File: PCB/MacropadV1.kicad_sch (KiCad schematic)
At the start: 17 parts, among them J1 Conn_01x04, SW1 SW_Push, SW10 RotaryEncoder_Switch, SW2 SW_Push, SW3 SW_Push, SW4 SW_Push, SW5 SW_Push, SW6 SW_Push, U1 MOUDLE-SEEEDUINO-XIAO

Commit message: just making sure i didnt forget anything
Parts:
- D1, D2, D3, D4, D5, D6: value D -> 1N4148; footprint Crystal:Crystal_SMD_G8-2Pin_3.2x1.5mm -> Diode_SMD:D_SOD-123
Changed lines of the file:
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@@
 			)
 		)
-		(property "Value" "D"
+		(property "Value" "1N4148"
 			(at 158.75 64.7699 90)
 			(show_name no)
@@
 			)
 		)
-		(property "Footprint" "Crystal:Crystal_SMD_G8-2Pin_3.2x1.5mm"
+		(property "Footprint" "Diode_SMD:D_SOD-123"
 			(at 156.21 63.5 0)
 			(hide yes)
@@
 			)
 		)
-		(property "Value" "D"
+		(property "Value" "1N4148"
 			(at 186.69 64.7699 90)
 			(show_name no)
@@
 			)
 		)
-		(property "Footprint" "Crystal:Crystal_SMD_G8-2Pin_3.2x1.5mm"
+		(property "Footprint" "Diode_SMD:D_SOD-123"
 			(at 184.15 63.5 0)
 			(hide yes)
@@
 			)
 		)
-		(property "Value" "D"
+		(property "Value" "1N4148"
 			(at 158.75 91.4399 90)
 			(show_name no)
@@
 			)
 		)
-		(property "Footprint" "Crystal:Crystal_SMD_G8-2Pin_3.2x1.5mm"
+		(property "Footprint" "Diode_SMD:D_SOD-123"
 			(at 156.21 90.17 0)
 			(hide yes)
@@
 			)
 		)
-		(property "Value" "D"
+		(property "Value" "1N4148"
 			(at 186.69 91.4399 90)
 			(show_name no)
@@
 			)
 		)
-		(property "Footprint" "Crystal:Crystal_SMD_G8-2Pin_3.2x1.5mm"
+		(property "Footprint" "Diode_SMD:D_SOD-123"
 			(at 184.15 90.17 0)
 			(hide yes)
@@
 			)
 		)
-		(property "Value" "D"
+		(property "Value" "1N4148"
 			(at 158.75 78.7399 90)
 			(show_name no)
@@
 			)
 		)
-		(property "Footprint" "Crystal:Crystal_SMD_G8-2Pin_3.2x1.5mm"
+		(property "Footprint" "Diode_SMD:D_SOD-123"
 			(at 156.21 77.47 0)
 			(hide yes)
@@
 			)
 		)
-		(property "Value" "D"
+		(property "Value" "1N4148"
 			(at 186.69 78.7399 90)
 			(show_name no)
@@
 			)
 		)
-		(property "Footprint" "Crystal:Crystal_SMD_G8-2Pin_3.2x1.5mm"
+		(property "Footprint" "Diode_SMD:D_SOD-123"
 			(at 184.15 77.47 0)
 			(hide yes)

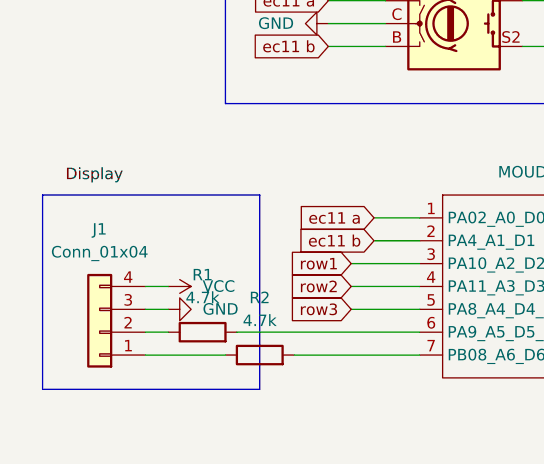
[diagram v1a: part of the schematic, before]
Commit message: fixed schematic display error
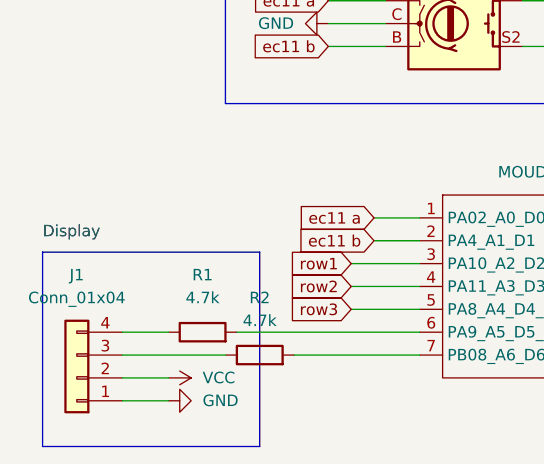
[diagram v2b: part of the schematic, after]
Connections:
- net GND: now also J1.1 (Pin_1); no longer J1.3 (Pin_3)
- net VCC: now also J1.2 (Pin_2); no longer J1.4 (Pin_4)
- net at R2.1: now also J1.3 (Pin_3); no longer J1.1 (Pin_1)
- net at R1.1: now also J1.4 (Pin_4); no longer J1.2 (Pin_2)
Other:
- moved on the sheet: J1
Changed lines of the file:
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@@
 	)
 	(rectangle
-		(start 33.02 77.47)
-		(end 57.15 99.06)
+		(start 33.02 83.82)
+		(end 57.15 105.41)
 		(stroke
 			(width 0)
@@
 	(wire
 		(pts
-			(xy 44.45 92.71) (xy 46.99 92.71)
-		)
-		(stroke
-			(width 0)
-			(type default)
-		)
-	)
-	(wire
-		(pts
 			(xy 67.31 90.17) (xy 74.93 90.17)
 		)
@@
 	(wire
 		(pts
-			(xy 44.45 95.25) (xy 53.34 95.25)
+			(xy 41.91 92.71) (xy 46.99 92.71)
 		)
 		(stroke
@@
 	(wire
 		(pts
-			(xy 44.45 90.17) (xy 46.99 90.17)
+			(xy 41.91 95.25) (xy 53.34 95.25)
 		)
 		(stroke
@@
 	(wire
 		(pts
+			(xy 41.91 97.79) (xy 46.99 97.79)
+		)
+		(stroke
+			(width 0)
+			(type default)
+		)
+	)
+	(wire
+		(pts
 			(xy 115.57 85.09) (xy 118.11 85.09)
 		)
@@
 	(wire
 		(pts
-			(xy 44.45 87.63) (xy 46.99 87.63)
-		)
-		(stroke
-			(width 0)
-			(type default)
-		)
-	)
-	(wire
-		(pts
 			(xy 184.15 86.36) (xy 187.96 86.36)
 		)
@@
 		(pts
 			(xy 184.15 59.69) (xy 187.96 59.69)
+		)
+		(stroke
+			(width 0)
+			(type default)
+		)
+	)
+	(wire
+		(pts
+			(xy 41.91 100.33) (xy 46.99 100.33)
 		)
 		(stroke
@@
 	)
 	(label "Display"
-		(at 35.56 76.2 0)
+		(at 33.02 82.55 0)
 		(effects
 			(font
@@
 	(symbol
 		(lib_id "Connector_Generic:Conn_01x04")
-		(at 39.37 92.71 180)
+		(at 36.83 97.79 180)
 		(unit 1)
 		(body_style 1)
@@
 		(fields_autoplaced yes)
 		(property "Reference" "J1"
-			(at 39.37 81.28 0)
+			(at 36.83 86.36 0)
 			(show_name no)
 			(do_not_autoplace no)
@@
 		)
 		(property "Value" "Conn_01x04"
-			(at 39.37 83.82 0)
+			(at 36.83 88.9 0)
 			(show_name no)
 			(do_not_autoplace no)
@@
 		)
 		(property "Footprint" "KicadMods:SSD1306-0.91-OLED-4pin-128x32"
-			(at 39.37 92.71 0)
+			(at 36.83 97.79 0)
 			(hide yes)
 			(show_name no)
@@
 		)
 		(property "Datasheet" ""
-			(at 39.37 92.71 0)
+			(at 36.83 97.79 0)
 			(hide yes)
 			(show_name no)
@@
 		)
 		(property "Description" "Generic connector, single row, 01x04, script generated (kicad-library-utils/schlib/autogen/connector/)"
-			(at 39.37 92.71 0)
+			(at 36.83 97.79 0)
 			(hide yes)
 			(show_name no)
@@
 	(symbol
 		(lib_id "power:VCC")
-		(at 46.99 87.63 270)
+		(at 46.99 97.79 270)
 		(unit 1)
 		(body_style 1)
@@
 		(fields_autoplaced yes)
 		(property "Reference" "#PWR03"
-			(at 43.18 87.63 0)
+			(at 43.18 97.79 0)
 			(hide yes)
 			(show_name no)
@@
 		)
 		(property "Value" "VCC"
-			(at 50.8 87.6299 90)
+			(at 50.8 97.7899 90)
 			(show_name no)
 			(do_not_autoplace no)
@@
 		)
 		(property "Footprint" ""
-			(at 46.99 87.63 0)
+			(at 46.99 97.79 0)
 			(hide yes)
 			(show_name no)
@@
 		)
 		(property "Datasheet" ""
-			(at 46.99 87.63 0)
+			(at 46.99 97.79 0)
 			(hide yes)
 			(show_name no)
@@
 		)
 		(property "Description" "Power symbol creates a global label with name \"VCC\""
-			(at 46.99 87.63 0)
+			(at 46.99 97.79 0)
 			(hide yes)
 			(show_name no)
@@
 	(symbol
 		(lib_id "power:GND")
-		(at 46.99 90.17 90)
+		(at 46.99 100.33 90)
 		(unit 1)
 		(body_style 1)
@@
 		(fields_autoplaced yes)
 		(property "Reference" "#PWR04"
-			(at 53.34 90.17 0)
+			(at 53.34 100.33 0)
 			(hide yes)
 			(show_name no)
@@
 		)
 		(property "Value" "GND"
-			(at 50.8 90.1699 90)
+			(at 50.8 100.3299 90)
 			(show_name no)
 			(do_not_autoplace no)
@@
 		)
 		(property "Footprint" ""
-			(at 46.99 90.17 0)
+			(at 46.99 100.33 0)
 			(hide yes)
 			(show_name no)
@@
 		)
 		(property "Datasheet" ""
-			(at 46.99 90.17 0)
+			(at 46.99 100.33 0)
 			(hide yes)
 			(show_name no)
@@
 		)
 		(property "Description" "Power symbol creates a global label with name \"GND\" , ground"
-			(at 46.99 90.17 0)
-			(hide yes)
-			(show_name no)
+			(at 46.99 100.33 0)
+			(hide yes)
+			(show_name no)

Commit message: added bom file
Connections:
- net col1: now also U1.3 (PA10_A2_D2); no longer U1.11 (PA6_A10_D10_MOSI)
- net col2: now also U1.4 (PA11_A3_D3); no longer U1.10 (PA5_A9_D9_MISO)
- net row1: now also U1.9 (PA7_A8_D8_SCK); no longer U1.3 (PA10_A2_D2)
- net row2: now also U1.10 (PA5_A9_D9_MISO); no longer U1.4 (PA11_A3_D3)
- net row3: now also U1.11 (PA6_A10_D10_MOSI); no longer U1.5 (PA8_A4_D4_SDA)
- net at R2.2: now also U1.6 (PA9_A5_D5_SCL); no longer U1.7 (PB08_A6_D6_TX)
- net at R1.2: now also U1.5 (PA8_A4_D4_SDA); no longer U1.6 (PA9_A5_D5_SCL)
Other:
- moved on the sheet: J1, R1, R2
